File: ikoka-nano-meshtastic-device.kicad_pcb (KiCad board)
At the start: 2 copper layers, 40 x 40 mm, 21 parts, among them J1 Qwiic_RA, J2 Solar, J3 Battery, J4 Battery, Q1 Q_PMOS_GSD, U1 Seeed Studio XIAO nRF52840, U2 E22-900M30S, U3 MT3608

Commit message: Sync symbol libraries
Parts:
- J1: footprint SparkFun-Connector:JST_SMD_1.0mm-4_RA -> SparkFun-Connector:JST_SMD_1.0mm-4_Black
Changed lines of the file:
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@@
 			)
 		)
-		(property "Description" ""
+		(property "Description" "Unpolarized capacitor"
 			(at 0 0 0)
 			(unlocked yes)
@@
 			)
 		)
-		(property ki_fp_filters "*C1206*")
+		(property ki_fp_filters "C_*")
 		(sheetname "Root")
 		(sheetfile "ikoka-nano-meshtastic-device.kicad_sch")
@@
 			(roundrect_rratio 0.188679)
 			(net 4 "GND")
-			(pinfunction "1")
 			(pintype "passive")
 		)
@@
 			(roundrect_rratio 0.188679)
 			(net 24 "VCC_E22")
-			(pinfunction "2")
 			(pintype "passive")
 		)
@@
 			)
 		)
-		(property "Description" ""
+		(property "Description" "Unpolarized capacitor"
 			(at 0 0 0)
 			(unlocked yes)
@@
 			)
 		)
-		(property ki_fp_filters "*C1206*")
+		(property ki_fp_filters "C_*")
 		(sheetname "Root")
 		(sheetfile "ikoka-nano-meshtastic-device.kicad_sch")
@@
 			(roundrect_rratio 0.188679)
 			(net 4 "GND")
-			(pinfunction "1")
 			(pintype "passive")
 		)
@@
 			(roundrect_rratio 0.188679)
 			(net 24 "VCC_E22")
-			(pinfunction "2")
 			(pintype "passive")
 		)
@@
 		)
 	)
-	(footprint "SparkFun-Connector:JST_SMD_1.0mm-4_RA"
+	(footprint "SparkFun-Connector:JST_SMD_1.0mm-4_Black"
 		(layer "F.Cu")
 		(at 150 114.5)
-		(tags "SparkFun")
+		(tags "SparkFun Qwiic Connector")
 		(property "Reference" "J1"
 			(at 0 1.8 0)
@@
 			)
 		)
-		(property "Footprint" "SparkFun-Connector:JST_SMD_1.0mm-4_RA"
+		(property "Footprint" "SparkFun-Connector:JST_SMD_1.0mm-4_Black"
 			(at 0 0 0)
 			(unlocked yes)
@@
 			(thermal_bridge_angle 0)
 		)
+		(model "${KIPRJMOD}/symbols/SparkFun-KiCad-Libraries/Footprints/SparkFun-3D-models/Connector/Qwiic-Horizontal.STEP"
+			(hide yes)
+			(offset
+				(xyz 0 -0.7 -0.3)
+			)
+			(scale
+				(xyz 1 1 1)
+			)
+			(rotate
+				(xyz -90 0 0)
+			)
+		)
+		(model "${KIPRJMOD}/symbols/SparkFun-KiCad-Libraries/Footprints/SparkFun-3D-models/Connector/JST_SMD_1.0mm-4.STEP"
+			(offset
+				(xyz 0 -0.7 -0.25)
+			)
+			(scale
+				(xyz 1 1 1)
+			)
+			(rotate
+				(xyz -90 0 0)
+			)
+		)
 		(model "${KIPRJMOD}/symbols/SparkFun-KiCad-Libraries/Footprints/SparkFun-3D-models/Connector/Qwiic-Horizontal-White.STEP"
+			(hide yes)
 			(offset
 				(xyz 0 -0.7 -0.3)
@@
 			(at 0 0 180)
 			(unlocked yes)
+			(layer "B.Fab")
+			(hide yes)
+			(effects
+				(font
+					(size 1 1)
+					(thickness 0.15)
+				)
+				(justify mirror)
+			)
+		)
+		(property "Description_1" "\nSX1262 868/915 MHz 1w SPI LoRa Module\n"
+			(at 0 0 180)
+			(unlocked yes)

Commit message: chore: Sync footprint libraries
Signed-off-by: Andrew Yong <me@ndoo.sg>
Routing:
- net SX126X_DIO1: track 20.5 -> 22.2 mm

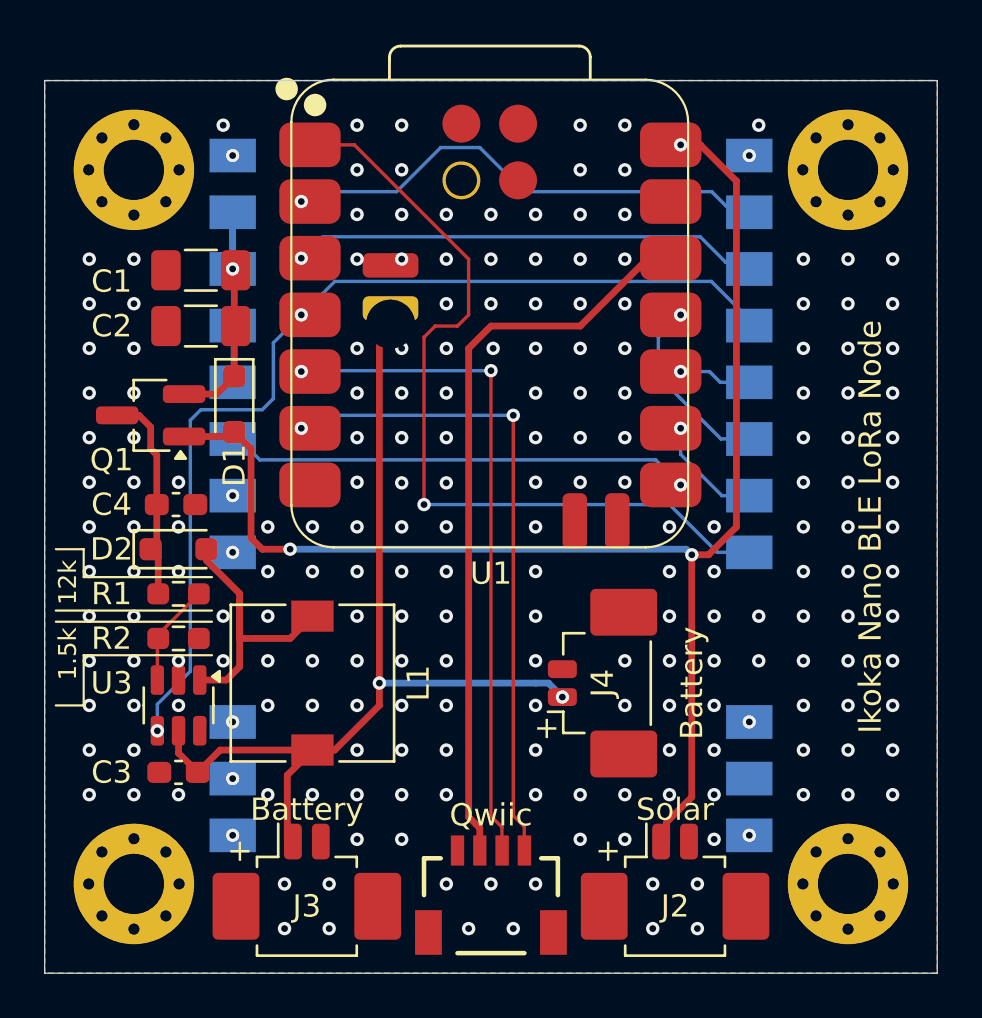
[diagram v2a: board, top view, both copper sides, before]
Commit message: feat: Improve DC-DC converter and power path
- Update R1 and R2 resistors to match Ikoka Handheld values (300kΩ, 39kΩ respectively)
- Change E22 capacitors to 2x 47µF instead of 2x 100µF
- Change P-MOSFET load switch to switch input to DC-DC boost so that E22 supply is constant even when switching to USB power
- Add 300k pulldown on MT3608L enable pin to prevent it floating when Meshtastic firmware is not running
- Layout for above changes
- Move connectors flush with PCB edge

Fixes #11

Signed-off-by: Andrew Yong <me@ndoo.sg>
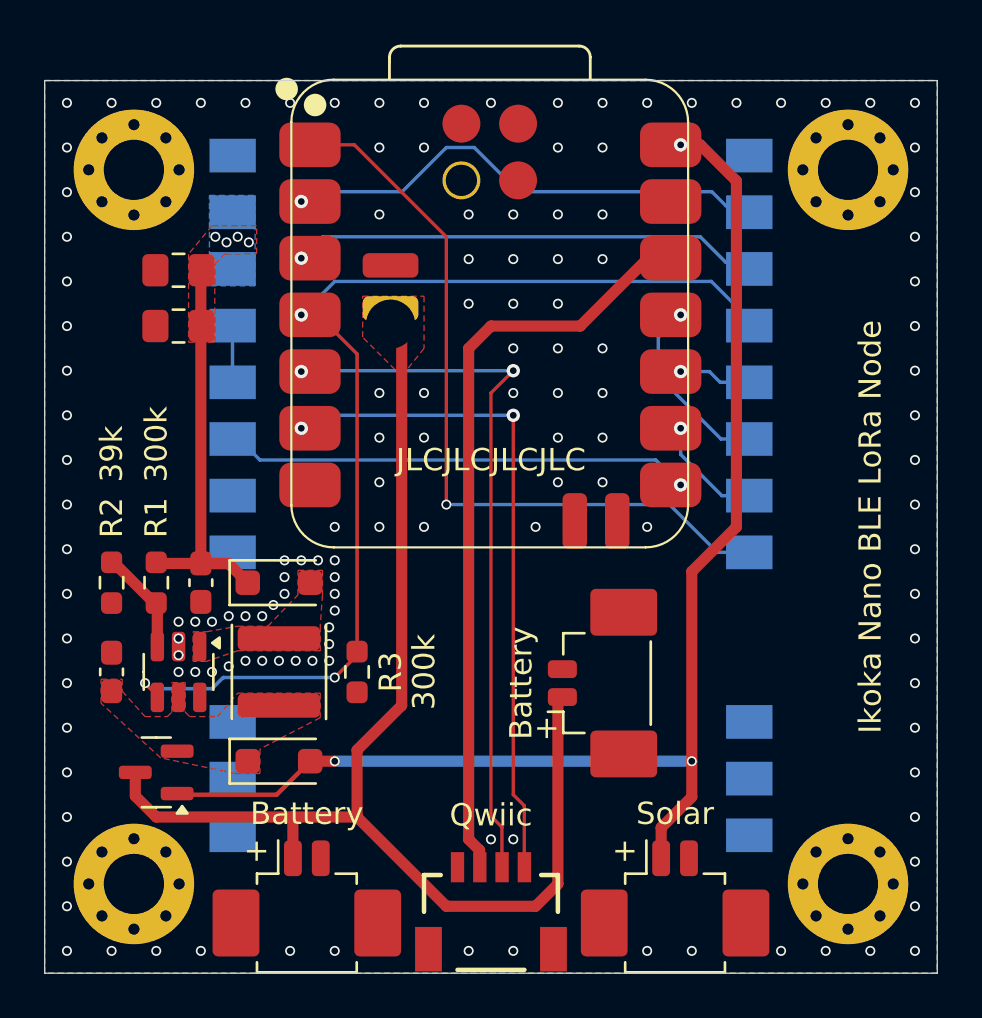
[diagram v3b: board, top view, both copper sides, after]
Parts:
- added R3: 300k, Resistor_SMD:R_0603_1608Metric_Pad0.98x0.95mm_HandSolder, F.Cu at (144.0, 106.5)
- C1, C2: value 100uF -> 47uF; footprint Capacitor_SMD:C_1206_3216Metric_Pad1.33x1.80mm_HandSolder -> Capacitor_SMD:C_0805_2012Metric_Pad1.18x1.45mm_HandSolder
- D1, D2: value D_Schottky -> DSK26; footprint Diode_SMD:D_SOD-323_HandSoldering -> Diode_SMD:D_SOD-123F
- L1: value 22uH -> FNR4026S220MT; footprint Inductor_SMD:L_SXN_SMDRI64 -> Inductor_SMD:L_Changjiang_FNR4026S
- Q1: value Q_PMOS_GSD -> AO3401A; footprint Package_TO_SOT_SMD:SOT-23_Handsoldering -> Package_TO_SOT_SMD:SOT-23
- R1: value 12k -> 300k
- R2: value 1.5k -> 39k
- U3: value MT3608 -> MT3608L
- moved D1 16.1 mm to (140.5, 110.5), turned to 0 degrees
- moved Q1 16.0 mm to (135.0, 111.0)
- moved C3 5.41 mm to (133.0, 106.5), turned to 90 degrees
- moved D2 4.74 mm to (140.5, 102.5)
- moved R2 3.91 mm to (133.0, 102.5), turned to -90 degrees
- moved C4 3.67 mm to (137.0, 102.5), turned to -90 degrees
- moved L1 1.58 mm to (140.5, 106.5)
- moved U3 1.50 mm to (136.0, 106.5)
- moved R1 1.12 mm to (135.0, 102.5), turned to 90 degrees
- moved C1 1.00 mm to (136.0, 88.5)
- moved C2 1.00 mm to (136.0, 91.0)
- moved J1 0.75 mm to (150.0, 115.2)
- moved J2 0.75 mm to (158.2, 117.2)
- moved J3 0.75 mm to (141.8, 117.2)
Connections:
- C3 pad 1: VBAT -> BOOST_IN
- C4 pad 1: 5V -> VCC_E22
- D1 pad 1: VCC_E22 -> BOOST_IN
- D2 pad 1: 5V -> VCC_E22
- L1 pad 1: VBAT -> BOOST_IN
- Q1 pad 2: VCC_E22 -> BOOST_IN
- Q1 pad 3: 5V -> VBAT
- R1 pad 1: 5V -> VCC_E22
- U1 pad 16: (no net) -> unconnected-(U1-GND-Pad16)
- U3 pad 5: VBAT -> BOOST_IN
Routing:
- net SW: track 15.0 -> 0.00 mm
- net VBAT: track 42.6 -> 56.6 mm, vias 2 -> 0
- net 5V: track 9.56 -> 0.00 mm
- net VCC_E22: track 10.5 -> 17.6 mm, vias 1 -> 4
- net SX126X_RESET: track 44.3 -> 48.8 mm, vias 2 -> 3
- net VBUS: track 62.0 -> 58.2 mm
- net SX126X_CS: track 37.5 -> 34.7 mm
- net I2C_SDA: track 30.7 -> 32.1 mm
- net GND: track 0.03 -> 0.00 mm, vias 213 -> 137
- added copper zone on F.Cu, net BOOST_IN
- added copper zone on F.Cu, net SW
- added copper zone on F.Cu, net VBAT
- added copper zone on B.Cu, net VCC_E22
- added copper zone on F.Cu, net VCC_E22

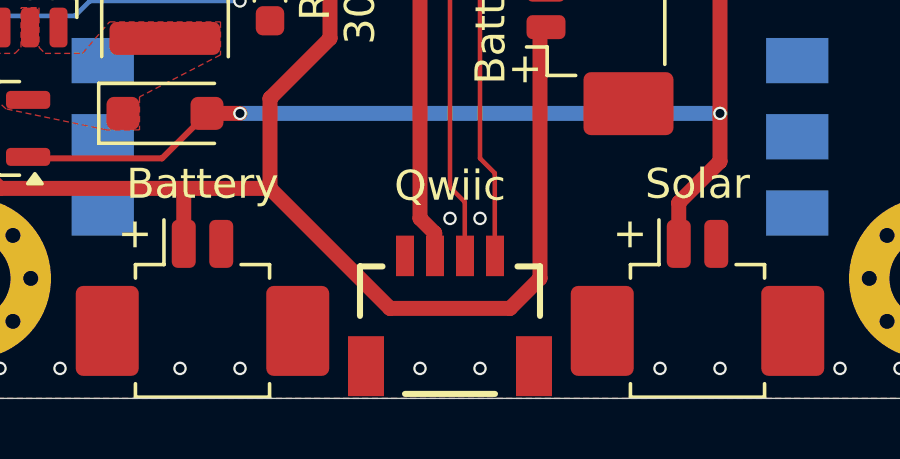
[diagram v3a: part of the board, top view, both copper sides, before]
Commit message: chore: Use correct Kicad connector symbols and ground MountingPins
Signed-off-by: Andrew Yong <me@ndoo.sg>
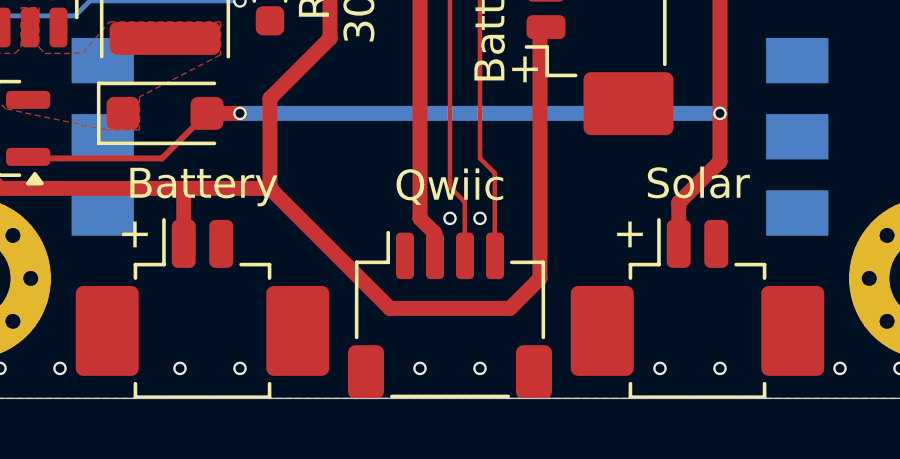
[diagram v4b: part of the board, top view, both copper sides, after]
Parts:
- J1: footprint SparkFun-Connector:JST_SMD_1.0mm-4_Black -> Connector_JST:JST_SH_SM04B-SRSS-TB_1x04-1MP_P1.00mm_Horizontal
- moved J1 2.00 mm to (150.0, 117.2)
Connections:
- J2 pad MP: (no net) -> GND
- J3 pad MP: (no net) -> GND
- J4 pad MP: (no net) -> GND
